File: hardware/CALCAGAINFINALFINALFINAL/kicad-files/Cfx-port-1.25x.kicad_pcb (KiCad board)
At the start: 4 copper layers, 65 x 135.9 mm, 104 parts, among them J2 USB_C_Receptacle_USB2.0_16P, J4 Conn_01x02, Q1 DMP3099L, Q2 2N7002, SW100 SW_SPST, SW101 SW_SPST, SW49 SW_SPST, SW52 SW_SPST, SW55 SW_SPST, SW56 SW_SPST, SW57 SW_SPST, SW58 SW_SPST, SW59 SW_SPST, SW60 SW_SPST, SW61 SW_SPST, SW62 SW_SPST, SW63 SW_SPST, SW64 SW_SPST, SW65 SW_SPST, SW66 SW_SPST, SW67 SW_SPST, SW68 SW_SPST, SW69 SW_SPST, SW70 SW_SPST, SW71 SW_SPST, SW72 SW_SPST, SW73 SW_SPST, SW74 SW_SPST, SW75 SW_SPST, SW76 SW_SPST, SW77 SW_SPST, SW78 SW_SPST, SW79 SW_SPST, SW80 SW_SPST, SW81 SW_SPST, SW82 SW_SPST, SW83 SW_SPST, SW84 SW_SPST, SW85 SW_SPST, SW86 SW_SPST, SW87 SW_SPST, SW88 SW_SPST, SW89 SW_SPST, SW90 SW_SPST, SW91 SW_SPST, SW92 SW_SPST, SW93 SW_SPST, SW94 SW_SPST, SW95 SW_SPST, SW96 SW_SPST, SW97 SW_SPST, SW98 SW_SPST, SW99 SW_SPST, U5 TP4056-42-ESOP8, U7 TCA9535DBR, U8 ESP32-S3-WROOM-2

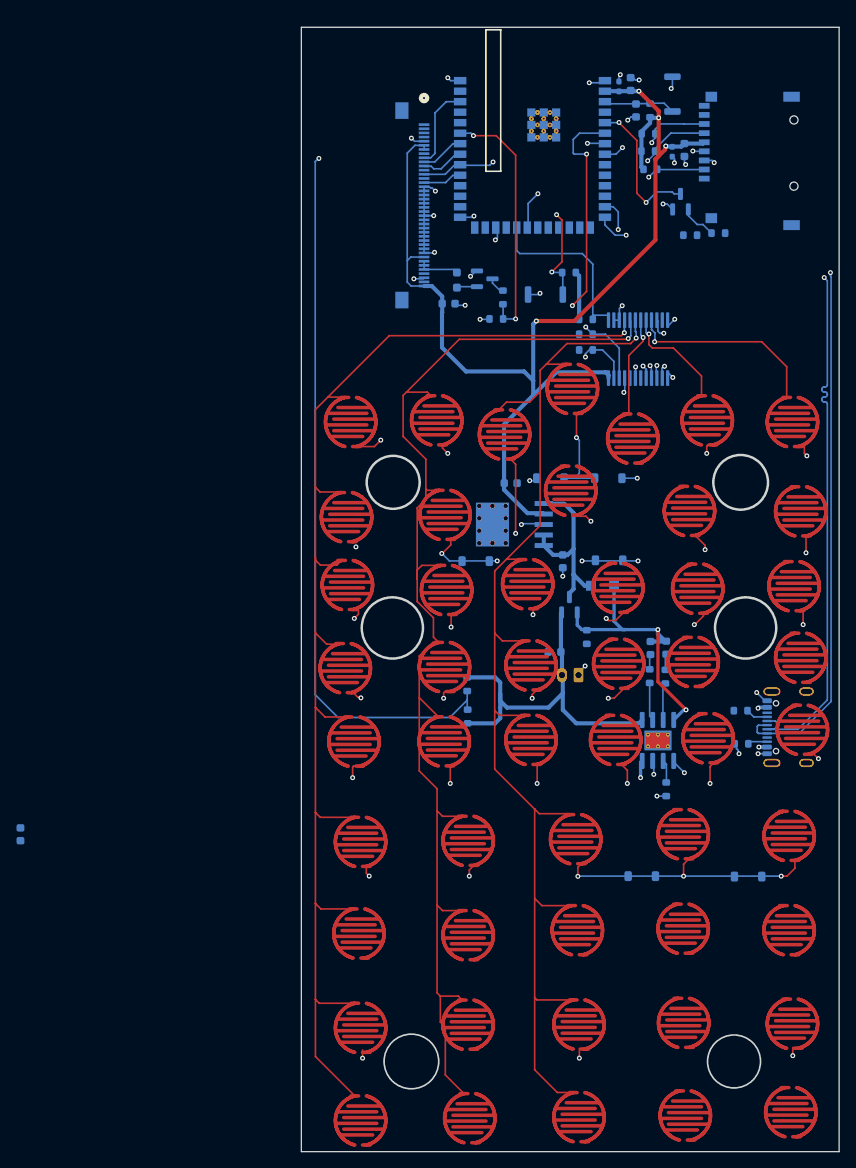
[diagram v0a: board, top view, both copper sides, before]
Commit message: v2 PCB ready for production: Cfx-port-1.25x final, drop v1 board files
- Cfx-port-1.25x.kicad_pcb: latest board save (FET + screen fixes)
- remove superseded Cfx-port v1 pcb/sch and stale DRC/ERC/tmp reports
- refresh netlist.ipc, project.db, project settings
Fab outputs (gerbers, CPL/BOM, production zip) intentionally untracked.
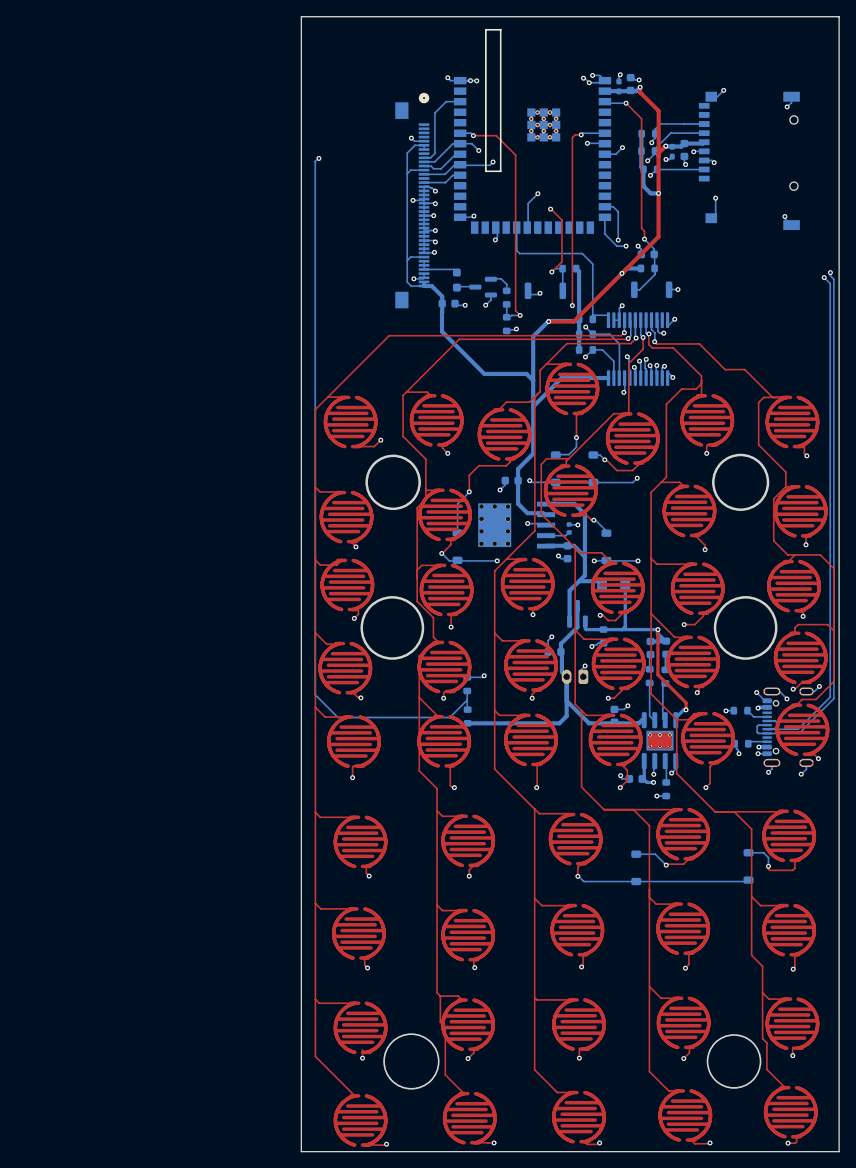
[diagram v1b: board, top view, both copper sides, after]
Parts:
- removed Q2: 2N7002, Package_TO_SOT_SMD:SOT-23
- removed R21, R22: 10k, Resistor_SMD:R_0603_1608Metric
- added C412: 10µF, Capacitor_SMD:C_0603_1608Metric, B.Cu at (137.9, 115.8)
- added res: 10nf 0402, Capacitor_SMD:C_0402_1005Metric, B.Cu at (129.9, 85.6)
- R12: value 1.2 -> 2.4k
- U7: value TCA9535DBR -> TCA9555DBR
- U8: value ESP32-S3-WROOM-2 -> ESP32-S3-WROOM-1
- r15: value 100k -> 10k
- rnein: renamed from REF**; value R_0603_1608Metric_Pad0.98x0.95mm_HandSolder -> 20ohm
- moved C6 73.2 mm to (135.3, 108.2), turned to -90 degrees
- moved B2 23.8 mm to (139.8, 56.7), turned to 0 degrees
- moved R8 19.1 mm to (139.4, 54.1), turned to 180 degrees
- moved C1 17.5 mm to (139.4, 52.5), turned to 180 degrees
- moved D8 2.81 mm to (116.4, 87.8), turned to -90 degrees
- moved D0 2.14 mm to (132.8, 78.3), turned to -90 degrees
- moved r15 2.03 mm to (134.0, 98.6)
- moved D2 1.66 mm to (134.4, 87.8), turned to -90 degrees
- moved Q1 1.47 mm to (130.9, 95.9)
- moved r11 1.41 mm to (122.3, 60.9), turned to 90 degrees
- moved D4 1.36 mm to (135.2, 92.3)
- moved D1 1.32 mm to (128.2, 78.3), turned to -90 degrees
- moved C4 1.24 mm to (129.7, 88.5)
- moved D7 1.23 mm to (151.6, 126.4), turned to -90 degrees
- moved D3 1.21 mm to (138.0, 126.6), turned to -90 degrees
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- renumbered C5 to C7, C5 to C8, D1 to D0, D3 to D7, D2 to D8, R6 to R10, R6 to R8, R6 to R9, REF** to c12, REF** to cat1, REF** to netj
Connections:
- D0 pad 1: /Keypad Matrix/R1 -> R1D2
- D1 pad 1: /Keypad Matrix/R1 -> R1D1
- D2 pad 1: /Keypad Matrix/R2 -> R2D2
- D3 pad 1: /Keypad Matrix/R6 -> r6d2
- D5 pad 1: VCC -> Net-(D15-A)
- D5 pad 2: Net-(D15-A) -> VCC
- D6 pad 1: VCC -> Net-(D20-A)
- D6 pad 2: Net-(D20-A) -> VCC
- D7 pad 1: /Keypad Matrix/R6 -> R6D1
- D8 pad 1: /Keypad Matrix/R2 -> R2D1
- LDO pad 4: pwr -> NR
- Q1 pad 2: /power-ic/BAT+ -> pwr
- Q1 pad 3: pwr -> /power-ic/BAT+
- SOt-23 pad 1: catode -> BL1
- SOt-23 pad 3: BL1 -> catode
- SW71 pad 1: /Keypad Matrix/R1 -> R1D1
- SW72 pad 1: /Keypad Matrix/R2 -> R2D1
- SW80 pad 1: /Keypad Matrix/R1 -> R1D2
- SW81 pad 1: /Keypad Matrix/R2 -> R2D2
- SW85 pad 1: /Keypad Matrix/R6 -> r6d2
- SW94 pad 1: /Keypad Matrix/R6 -> R6D1
- r14 pad 2: /power-ic/BAT+ -> GND
- toes pad 4: SCL -> /esp32-s3 pinout/SCK
- toes pad MNT1: (no net) -> GND
- toes pad MNT2: (no net) -> GND
- toes pad MNT3: (no net) -> GND
- toes pad MNT4: (no net) -> GND
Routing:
- net /Keypad Matrix/R9: track 0.00 -> 196.5 mm, vias 0 -> 6
- net /Keypad Matrix/R7: track 0.00 -> 177.6 mm, vias 0 -> 6
- net /Keypad Matrix/C4: track 12.3 -> 143.1 mm
- net /Keypad Matrix/C5: track 13.5 -> 143.5 mm
- net /Keypad Matrix/C6: track 23.5 -> 79.7 mm
- net GND: track 50.9 -> 86.5 mm, vias 31 -> 54
- net /esp32-s3 pinout/SCK: track 5.27 -> 35.7 mm, vias 0 -> 2
- net /Keypad Matrix/R4: track 116.7 -> 142.8 mm, vias 5 -> 7
- net /Keypad Matrix/R2: track 150.8 -> 125.6 mm, vias 10 -> 8
- net en: track 8.19 -> 27.6 mm, vias 0 -> 2
- net CAM_PWDN_G: track 17.5 -> 0.00 mm, vias 2 -> 0
- net SCL: track 52.9 -> 36.7 mm, vias 4 -> 3
- net R2D1: track 0.00 -> 13.6 mm, vias 0 -> 1
- net R6D1: track 0.00 -> 8.36 mm, vias 0 -> 1
- net 3V3: track 116.9 -> 124.6 mm, vias 4 -> 5
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- added copper zone on In1.Cu, net GND
- removed copper zone on In2.Cu, net GND
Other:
- board size 65 x 135.9 mm -> 65 x 137.2 mm
- board text removed: "1"
- board text removed: "gnd"
